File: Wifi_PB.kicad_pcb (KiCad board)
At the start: 2 copper layers, 100 x 49.7 mm, 208 parts, among them P1 CONN_01X02, P10 CONN_01X01, P12 CONN_01X04, P13 CONN_01X04, P14 CONN_01X04, P15 USB_MINI, P16 CONN_01X01, P17 CONN_01X01, P18 CONN_01X01, P19 CONN_01X01, P2 CONN_01X03, P3 CONN_01X03, P4 CONN_01X03, P5 CONN_01X03, P6 CONN_01X01, P7 CONN_01X01, P8 CONN_01X01, P9 CONN_01X01, Q1 SMBT3904, Q10 BC849, Q11 NX2301P, Q2 SMBT3904, Q3 BSS138, Q4 BSS138, Q5 SMBT3904, Q6 SMBT3904, Q7 SMBT3904, Q8 SMBT3904, Q9 SMBT3904, SW1 Pulsador_2p, SW2 Pulsador_2p, SW3 Pulsador_2p, SW4 Pulsador_2p, U1 MCP73831T, U10 Matriz_5x7_Anodo_Filas, U11 40106, U12 MCP1640, U2 LD1117S33TR, U3 CH340G, U4 ESP8266, U5 MMA7660FC, U6 MCP23017, U7 MCP23017, U8 MCP3204, U9 PCA9551, Y1 Cristal

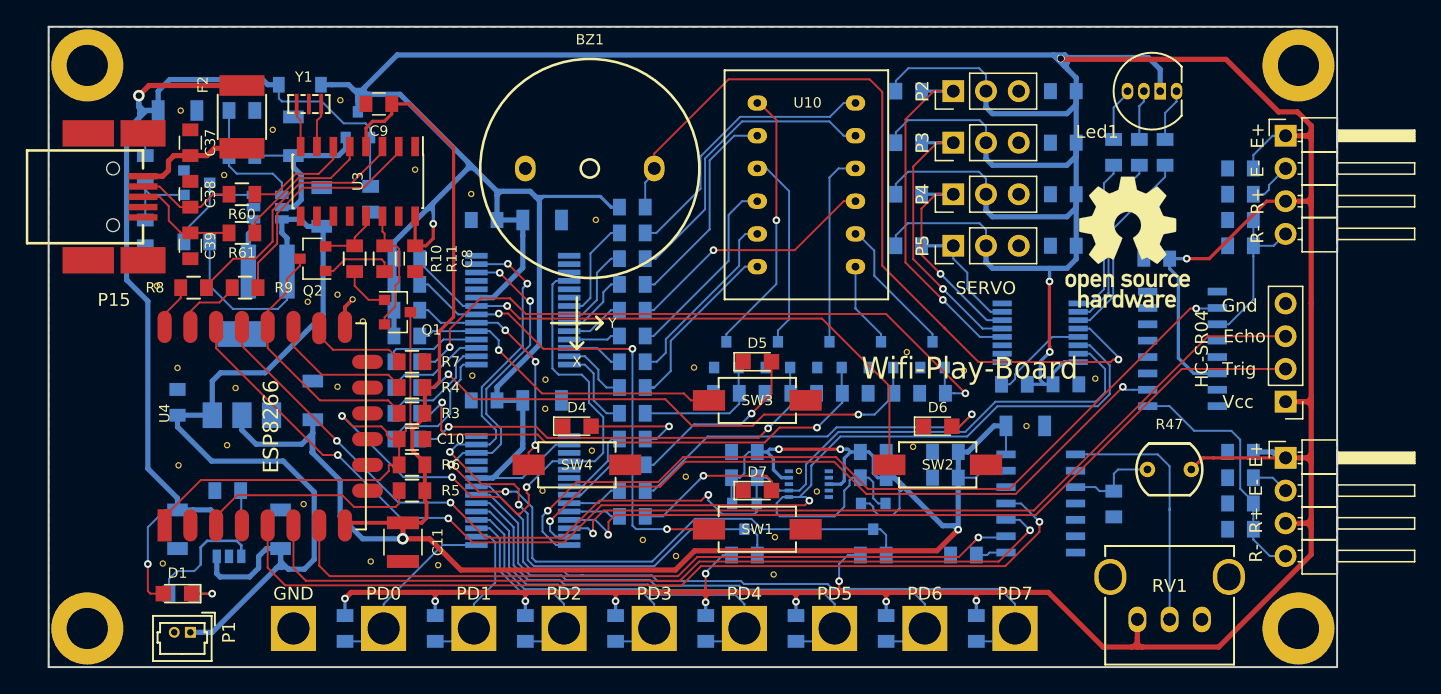
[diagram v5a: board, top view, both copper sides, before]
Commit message: correcciones en serigrafias sobre pads
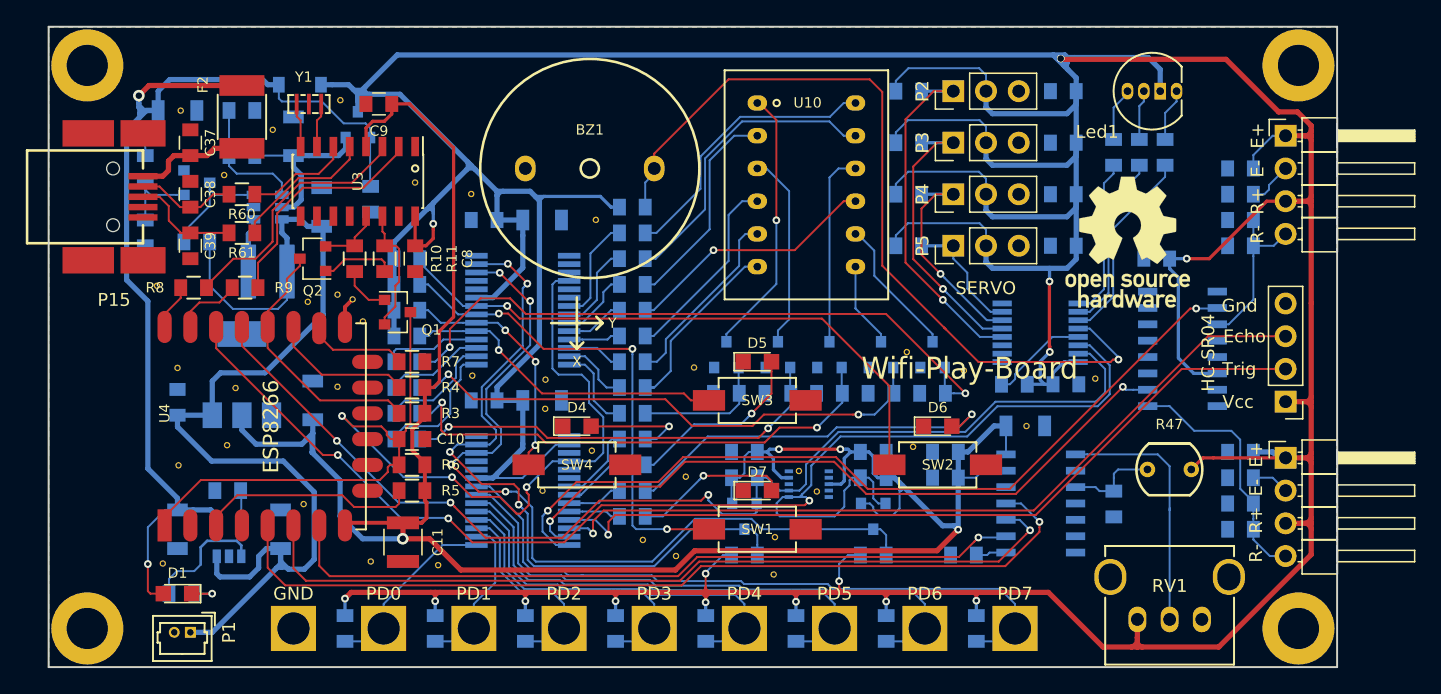
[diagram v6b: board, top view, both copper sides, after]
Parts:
- moved Gnd-Via 1.00 mm to (82.4, 47.1)
